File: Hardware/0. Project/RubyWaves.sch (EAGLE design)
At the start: 26 parts, among them J2 CORTEX_DEBUGPTH, U1 MAX32664, U2 MAX30102, U3 30102, U4 NRF52832, Y1 32MHz, Y2 32.768kHz

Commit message: WIP
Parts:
- removed J1: (no value), SparkFun-Connectors:ARDUINO_SERIAL_PROGRAMPTH
- added C10, C20, C3, C30: 100nF, My-RLC:C_0603
- added C15, C19: 22uF x 16V, rcl:C-EUC0805
- added C2, C32: 10uF, My-RLC:C_0603
- added C31: 4.7nF, My-RLC:C_0603
- added C5, C6: 1uF, My-RLC:C_0603
- added C7, C9: 22pF, My-RLC:C_0603
- added CN1: USB 3.2 Gen 2 Type C Receptacle, USB C CONNECOTR:USB4080-03-A
- added CN2: Lithium Ion Polymer, Battery:BATTERYJST-2
- added D1: SS16, diode:SUPPRESSOR-SMBJ
- added L1: 22 uH, Inductor:INDUCTOR
- added Q2, Q3: SI2374DS, SI2374DS:SI2374DSSOT23
- added R1: 0R, My-RLC:R_0603
- added R10, R11: 5k1, My-RLC:R_0603
- added R12, R13, R15, R16, R17: 1M, My-RLC:R_0603
- added R2, R3, R4, R7: 4k7, My-RLC:R_0603
- added R6: 15k (±1%), rcl:R-EU_R0603
- added R8: 2k, My-RLC:R_0603
- added R9: 470R, My-RLC:R_0603
- added U5: MCP73831/2, adafruit:MCP73831/OT
- added U6: S-8261ACMMD-G4MT2U, SamacSys_Parts:S-8261ACMMD-G4MT2U
- added Y3: 32.768 kHz, crystal-geyer_V1_0:CRYSTAL-MINI
- R5: value 4.7k -> 110k (±1%); device SparkFun-Resistors:4.7KOHM-0603-1/10W-1% -> rcl:R-EU_R0603
- U3: value 30102 -> MT3608; device SparkFun-Sensors:MAX3010X-30102 -> MT3608:MT3608
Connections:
- removed net !INT: R5.1, U3.!INT
- removed net 3.3V: R5.2, U3.VLED+@10, U3.VLED+@9
- removed net LV_SCL: U3.SCL
- removed net LV_SDA: U3.SDA
- new net !BIO_SENSOR_TRIGGER_INTERRUPT: R2.1, U1.HR_INT, U2.!INT
- new net 0V1: Q3.S, R16.1, R7.1, R8.1, U5.VSS
- new net 5.0V: C19.1, C2.1, D1.C, R5.2, U2.VLED+
- new net ADC_BATTERY_VOLTAGE: R15.1, R16.2
- new net DGND: C2.2, R1.1, U2.PGND
- new net GPIO_BATTERY_CHARGING_STATUS: U5.STAT
- new net GPIO_USB_DETECT: R13.1, R17.2
- new net N$10: CN1.CC1, R10.1
- new net N$14: C31.2, CN1.SHIELD, R12.1
- new net N$21: CN1.CC2, R11.1
- new net N$26: R7.2, U5.PROG
- new net N$27: Q3.G, U6.CO
- new net N$29: R8.2, U6.VM
- new net N$3: C6.1, U1.VCORE
- new net N$31: C20.1, R9.2, U6.VDD
- new net N$32: C20.2, CN2.GND, Q2.S, U6.VSS
- new net N$4: D1.A, L1.2, U3.SW
- new net N$5: R5.1, R6.2, U3.FB
- new net N$7: Q2.G, U6.DO
- new net N$9: Q2.D, Q3.D
- new net VBAT: C15.1, CN2.VDD, L1.1, R15.2, R9.1, U3.EN, U3.IN, U5.VBAT
- new net VSS: C10.2, C3.2, C5.2, C6.2, C7.2, C9.2, R1.2, U1.VSS, U2.VSS
- new net VUSB: C30.2, C32.2, CN1.VBUS_A, CN1.VBUS_B, R13.2, U5.VDD
- new net XTAL_IN: C7.1, U1.XIN, Y3.1
- new net XTAL_OUT: C9.1, U1.XOUT, Y3.2
- net 0V: now also C30.1, C31.1, C32.1, CN1.GND_A, CN1.GND_B, R10.2, R11.2, R12.2, R17.1; no longer J1.GND
- net 1.8V: now also C10.1, C3.1, C5.1, R2.2, R3.2, R4.2, U1.VDD, U2.VDD; no longer U3.VDD
- net GND: now also C15.2, C19.2, R6.1; no longer U3.PGND
- net MCU_ICSP_UART_RX: no longer J1.RXI
- net MCU_ICSP_UART_TX: no longer J1.TXO
- net N$1: now also R4.1
- net N$2: now also R3.1
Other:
- note added: "15mA to 500mA max."
- note added: "2.1μA max."
- note added: "3.7V ~ 4.2V 230mAh"
- note added: "7μA max."
- note added: "I-REG [mA] = 1000V / R-PROG"
- note added: "Overcharge = 4.325V"
- note added: "Overdischarge = 3.000V"
- note removed: "Logic is 1.8V 3.3V for LED Driver"
- moved on the sheet: C17, C23, E1, L2, U1, U2

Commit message: New board reference added
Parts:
- removed C20: 100nF, My-RLC:C_0603
- removed Q2, Q3: SI2374DS, SI2374DS:SI2374DSSOT23
- removed R8: 2k, My-RLC:R_0603
- removed R9: 470R, My-RLC:R_0603
- removed U6: S-8261ACMMD-G4MT2U, SamacSys_Parts:S-8261ACMMD-G4MT2U
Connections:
- removed net N$27: Q3.G, U6.CO
- removed net N$29: R8.2, U6.VM
- removed net N$31: C20.1, R9.2, U6.VDD
- removed net N$32: C20.2, CN2.GND, Q2.S, U6.VSS
- removed net N$7: Q2.G, U6.DO
- removed net N$9: Q2.D, Q3.D
- net 0V1: now also CN2.GND; no longer Q3.S, R8.1
- net VBAT: no longer R9.1
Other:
- note removed: "7μA max."
- note removed: "Overcharge = 4.325V"
- note removed: "Overdischarge = 3.000V"
- moved on the sheet: C30, C31, C32, CN1, R10, R11, R12, R13, R17, R7, U5

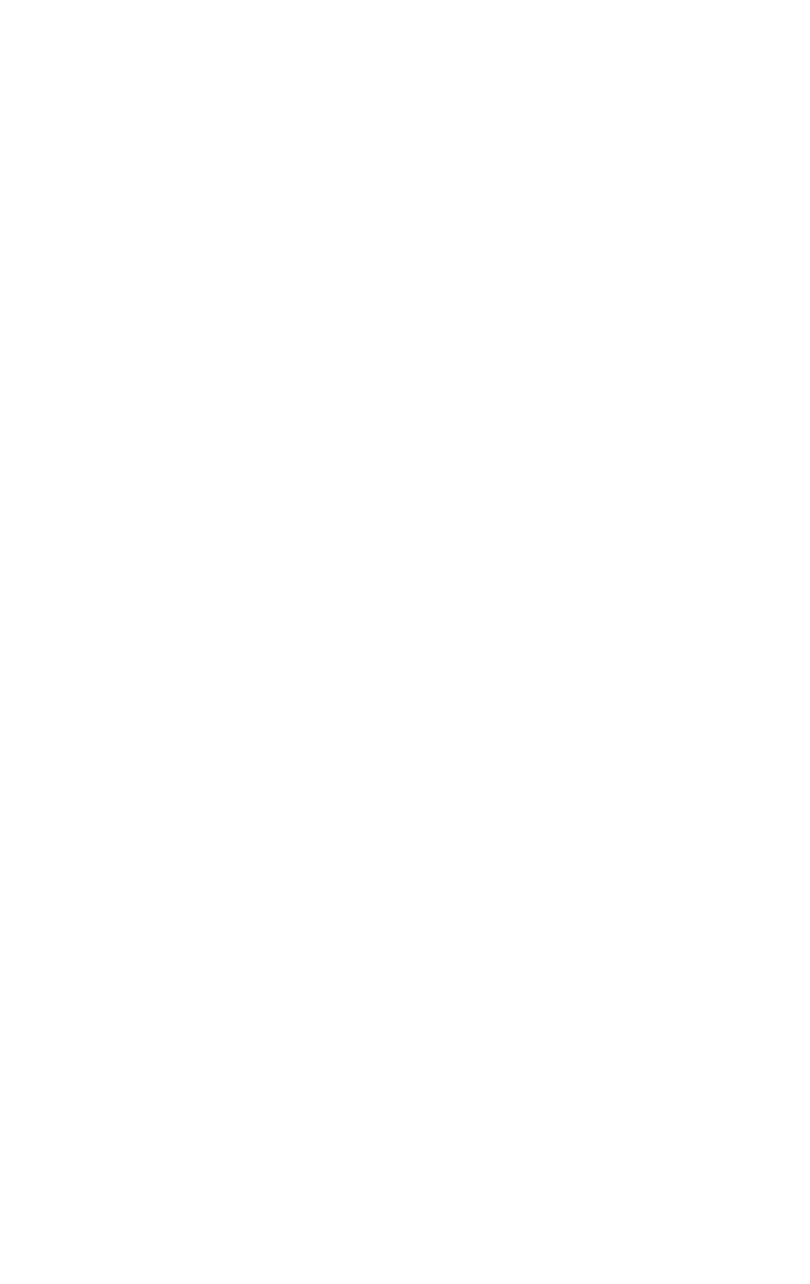
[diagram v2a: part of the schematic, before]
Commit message: PMIC added
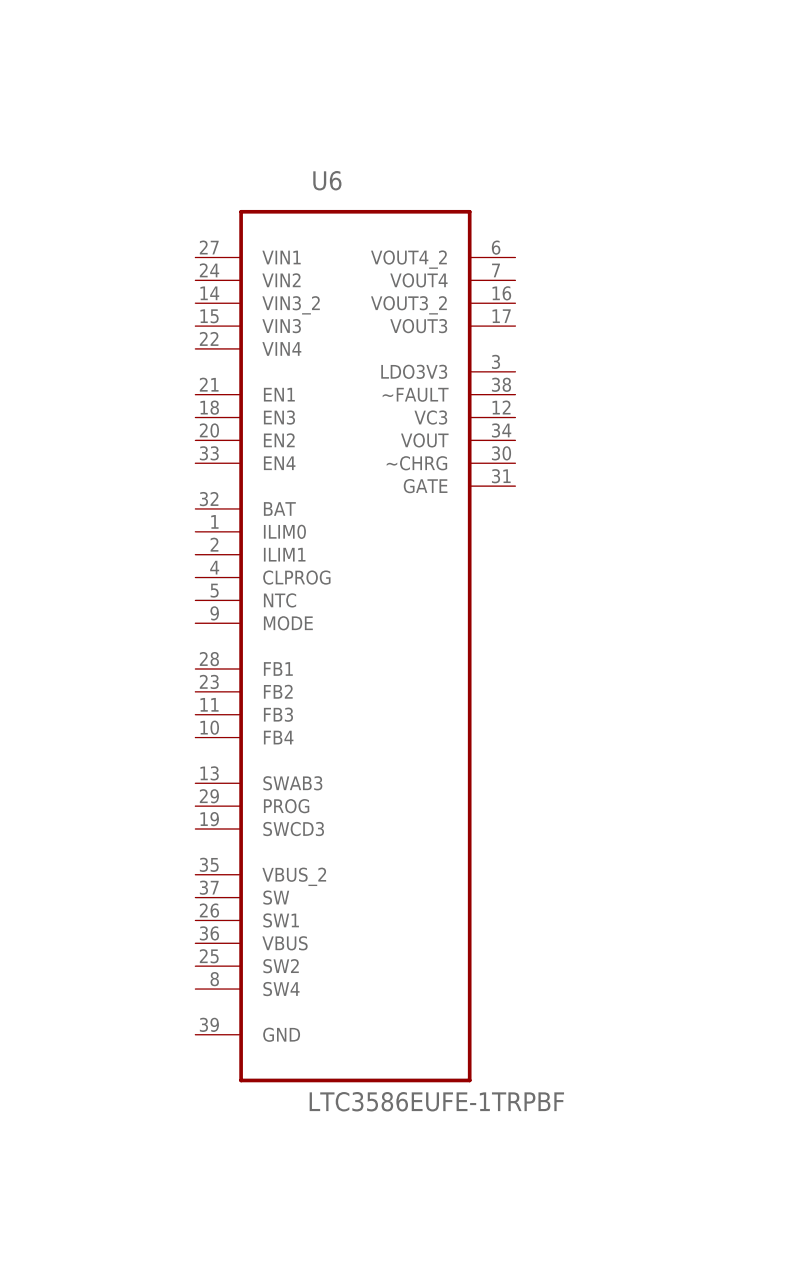
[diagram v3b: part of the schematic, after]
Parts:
- added U6: LTC3586EUFE-1TRPBF, LTC3586:LTC3586EUFE-1TRPBF
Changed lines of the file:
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@@
 <setting verticaltext="up"/>
 </settings>
-<grid distance="0.025" unitdist="inch" unit="inch" style="lines" multiple="1" display="no" altdistance="0.01" altunitdist="inch" altunit="inch"/>
+<grid distance="0.1" unitdist="inch" unit="inch" style="lines" multiple="1" display="no" altdistance="0.01" altunitdist="inch" altunit="inch"/>
 <layers>
 <layer number="1" name="Top" color="4" fill="1" visible="no" active="no"/>
@@
 <part name="SUPPLY22" library="My-Supply" deviceset="0V" device=""/>
 <part name="SUPPLY15" library="My-Supply" deviceset="5.0V" device=""/>
+<part name="U6" library="LTC3586" deviceset="LTC3586EUFE-1TRPBF" device=""/>
 </parts>
 <sheets>
@@
 <attribute name="VALUE" x="368.3254" y="-109.855" size="1.778" layer="96" align="center"/>
 </instance>
+<instance part="U6" gate="A" x="292.1" y="152.4" smashed="yes">
+<attribute name="NAME" x="287.1978" y="200.533" size="2.0828" layer="95" ratio="10" rot="SR0"/>
+<attribute name="VALUE" x="286.766" y="98.1964" size="2.0828" layer="96" ratio="10" rot="SR0"/>
+</instance>
 </instances>
